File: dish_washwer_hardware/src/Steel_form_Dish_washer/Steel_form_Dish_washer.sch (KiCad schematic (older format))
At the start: 64 parts, among them J1 RTD_TANK_SENSOR, J2 RTD_BOILER_SENSOR, J3 AC_PWR_IN, J4 MAG_DOOR_SENSOR, J5 Conn_01x04_Male, J6 Conn_01x04_Male, J7 FLOAT SWITCH CONN, J8 3-1734592-0, Q1 BSS138, Q2 BSS138, SW1 SW_Push, SW2 SW_Push, SW3 SW_Push, U1 ATmega2560-16AU, U2 LM1117-3.3, U3 MAX31865ATP+T, U4 MAX31865ATP+T, U5 TL1240GQ1JCLR, U6 TL1240GQ1JCLR, Y1 C3E-16.000-12-1010-M

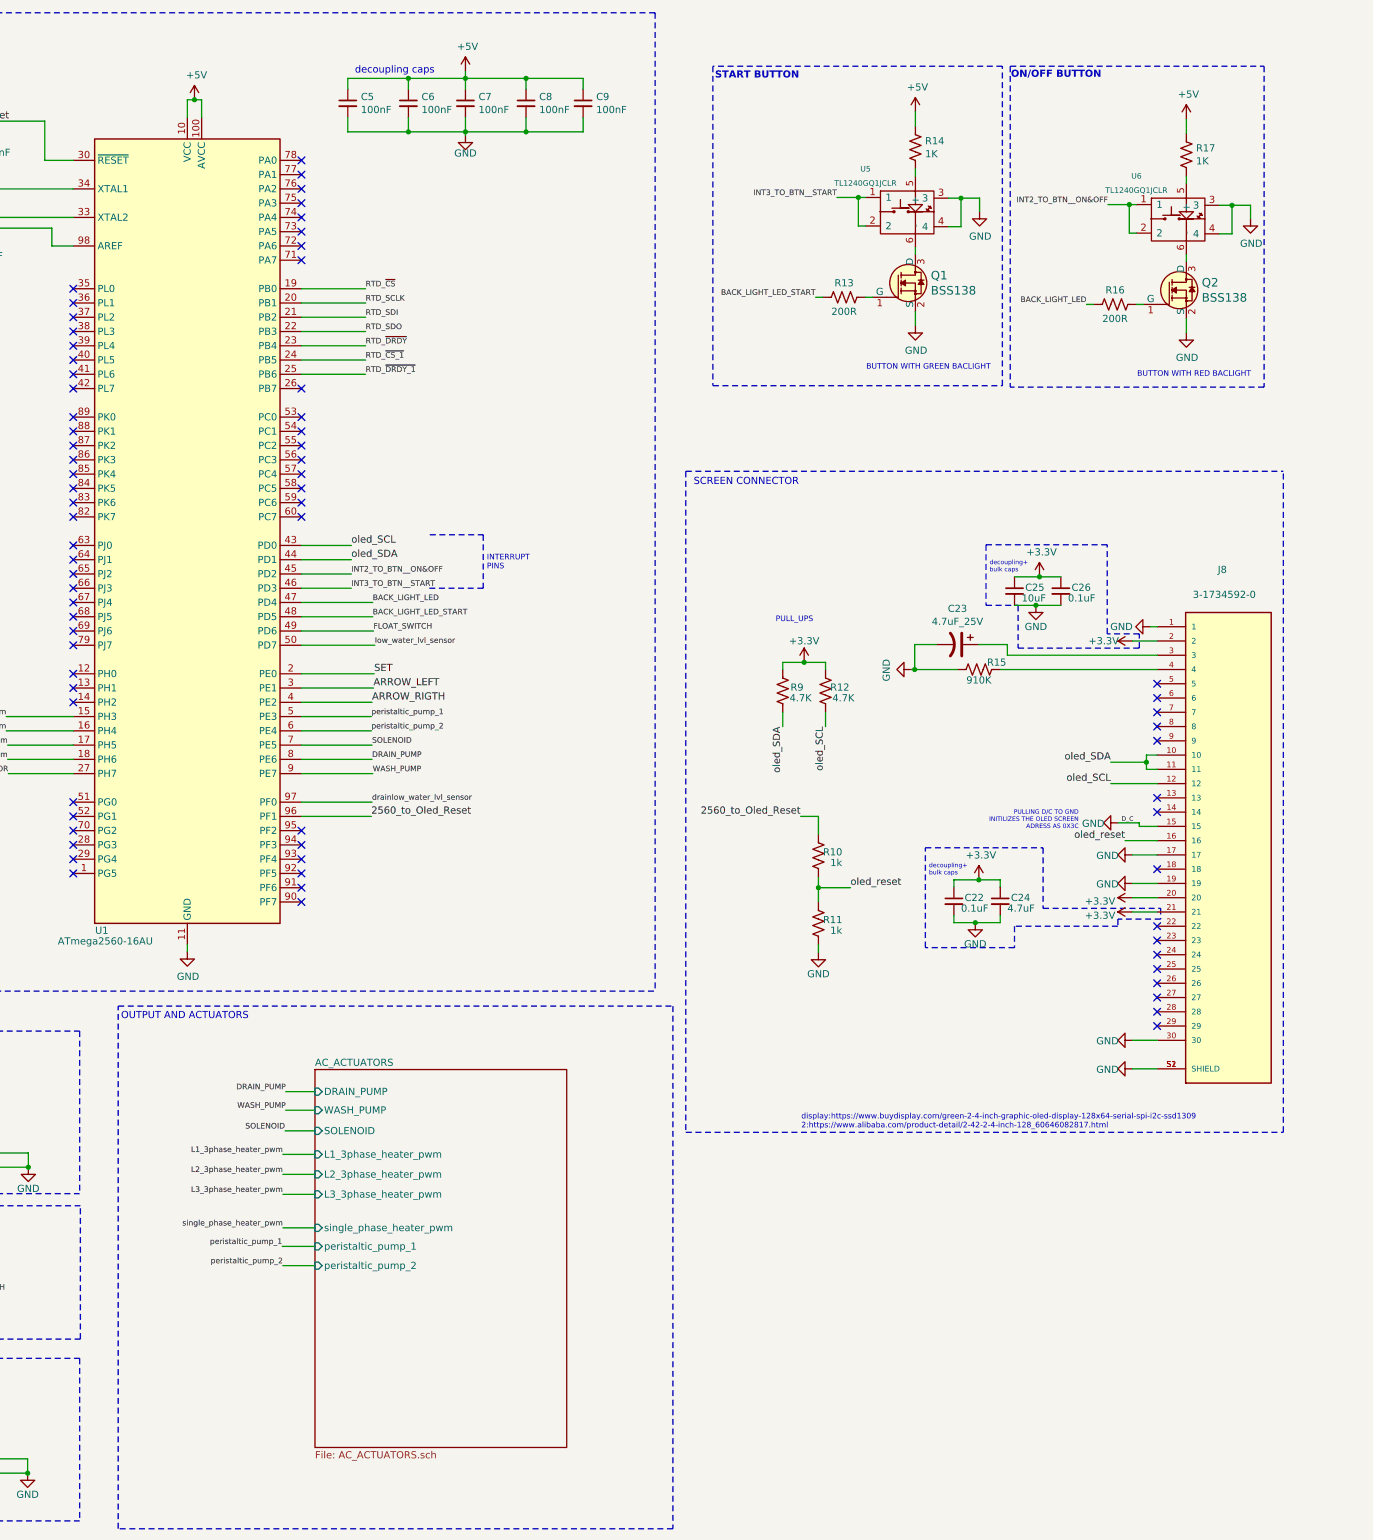
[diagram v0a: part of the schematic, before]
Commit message: update schematic zero detect circuit
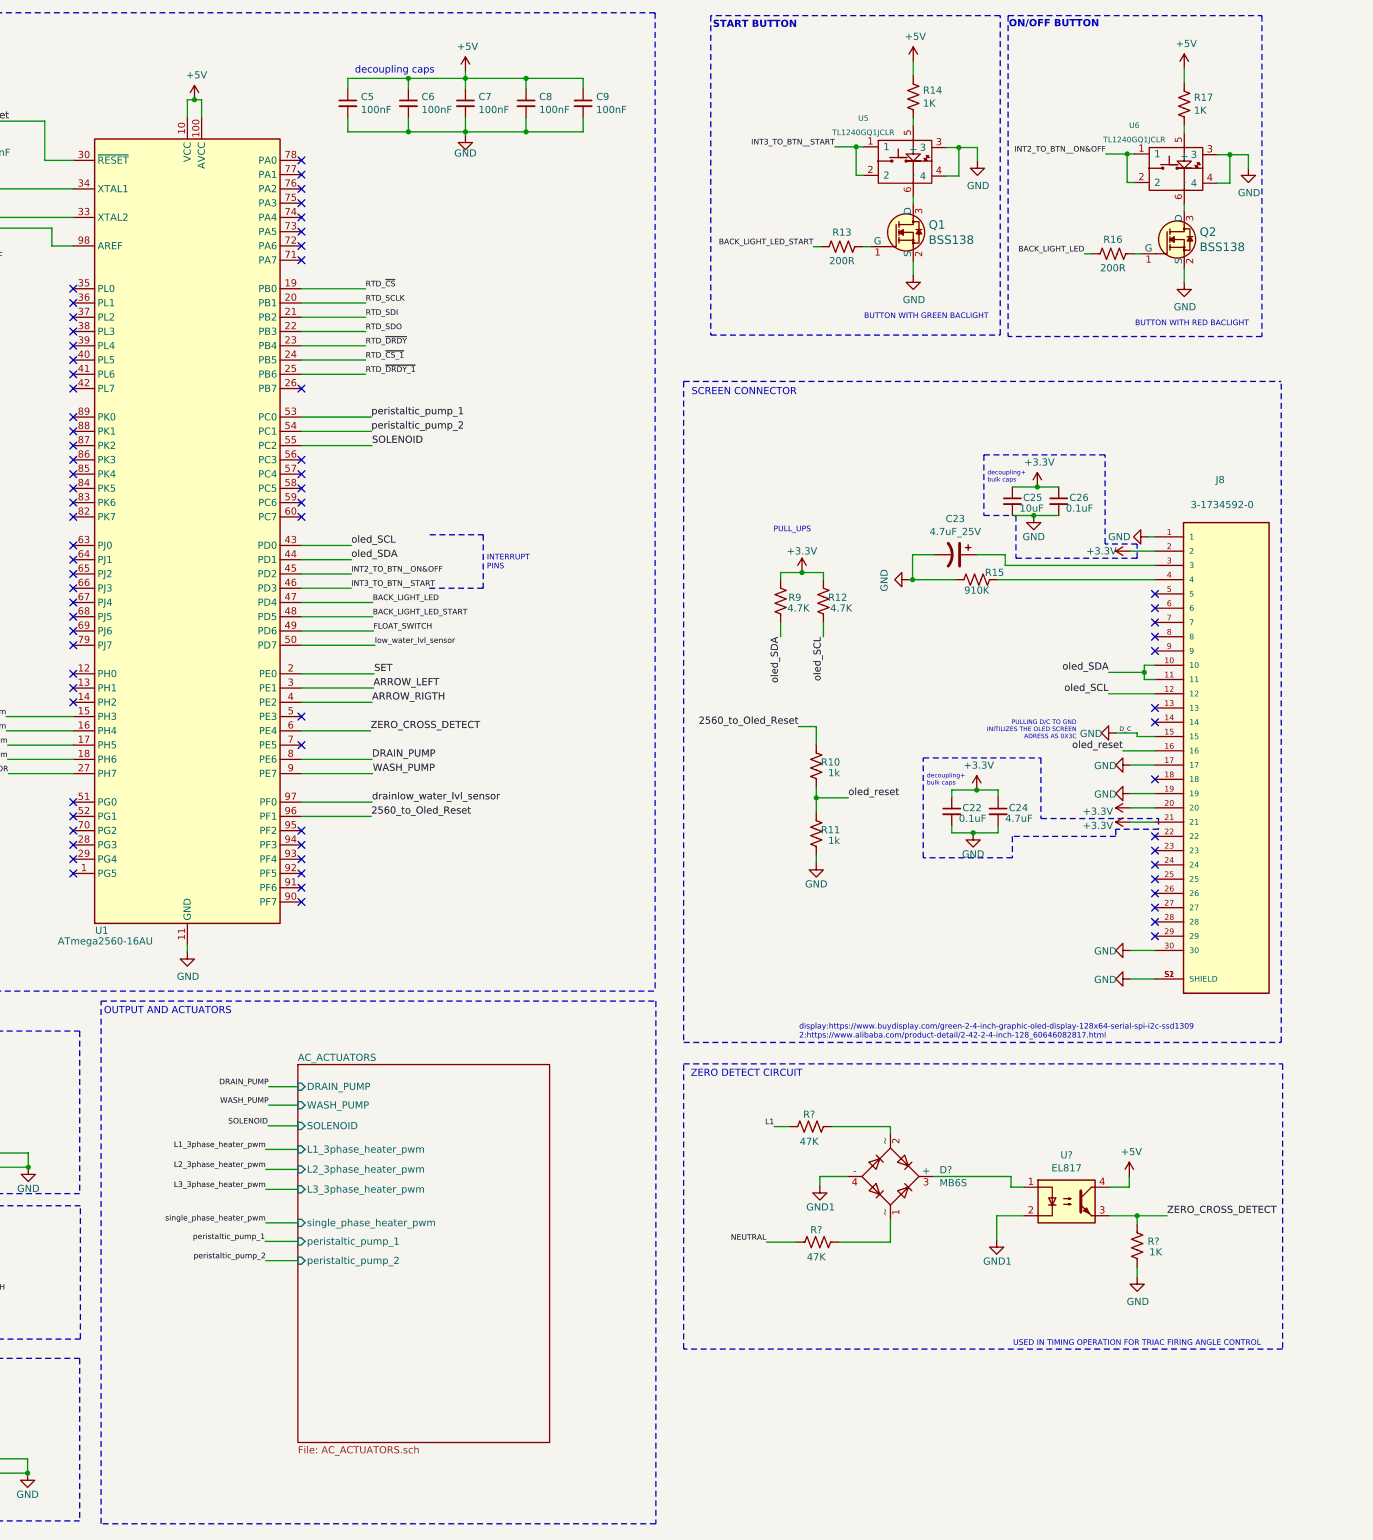
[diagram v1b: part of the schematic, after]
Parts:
- added D?: MB6S, Package_TO_SOT_SMD:TO-269AA, symbol Diode_Bridge:MB6S
- added R? (x2): 47K, symbol Device:R_US
- added R?: 1K, symbol Device:R_US
- added U?: EL817, Package_DIP:DIP-4_W7.62mm, symbol Isolator:EL817
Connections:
- net +5V: now also U?.4
- net GND: now also R?.1
- net L1: now also R?.1
- net NEUTRAL: now also R?.1
- net SOLENOID: now also U1.55 (PC2); no longer U1.7 (PE5)
- net peristaltic_pump_1: now also U1.53 (PC0); no longer U1.5 (PE3)
- net peristaltic_pump_2: now also U1.54 (PC1); no longer U1.6 (PE4)
- new net: D?.1 (~~), R?.2
- new net: D?.2 (~~), R?.2
- new net: D?.3 (+), U?.1
- new net GND1: D?.4 (-), U?.2
- new net ZERO_CROSS_DETECT: R?.2, U1.6 (PE4), U?.3
- no-connect marks 72 -> 71
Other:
- note added: "USED IN TIMING OPERATION FOR TRIAC FIRING ANGLE CONTROL"
- note added: "ZERO DETECT CIRCUIT"
- moved on the sheet: C22, C23, C24, C25, C26, J8, Q1, Q2, R10, R11, R12, R13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

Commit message: footprint assignment and Varistor
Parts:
- added RV1, RV2, RV3: VDR-14D181K, Varistor:RV_Disc_D16.5mm_W6.7mm_P7.5mm, symbol Device:Varistor
- C1, C10, C11, C12, C13, C14, C15, C16, C17, C18, C19, C2, C20, C21, C22, C24, C25, C26, C3, C4, C5, C6, C7, C8, C9: footprint (none) -> Capacitor_SMD:C_0402_1005Metric
- C23: footprint (none) -> Capacitor_Tantalum_SMD:CP_EIA-3528-21_Kemet-B
- J1, J2: footprint (none) -> Connector_JST:JST_EH_S3B-EH_1x03_P2.50mm_Horizontal
- J3: footprint (none) -> greencharge-footprints:387207505
- J4, J7: footprint (none) -> Connector_JST:JST_EH_S2B-EH_1x02_P2.50mm_Horizontal
- J5, J6: footprint (none) -> Connector_JST:JST_EH_S4B-EH_1x04_P2.50mm_Horizontal
- R1, R10, R11, R12, R13, R14, R15, R16, R17, R2, R3, R5, R6, R7, R8, R9: footprint (none) -> Resistor_SMD:R_0402_1005Metric
- R36, R37: renamed from R?; footprint (none) -> Resistor_SMD:R_0805_2012Metric
- R38: renamed from R?; footprint (none) -> Resistor_SMD:R_0402_1005Metric
- R4: value 1K -> 200R; footprint (none) -> Resistor_SMD:R_0402_1005Metric
- gave numbers to parts that had none: 2
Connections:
- net L1: now also RV1.1
- net L2: now also RV2.1
- net L3: now also RV3.1
- net NEUTRAL: now also RV1.2, RV2.2, RV3.2
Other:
- moved on the sheet: J3

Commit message: updated dishwasher schematic
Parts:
- removed J8: 3-1734592-0, greencharge-footprints:TE_3-1734592-0, symbol 3-1734592-0:3-1734592-0
- added J16: Conn_01x31, greencharge-footprints:oled_128x64_GDOE0240G, symbol Connector_Generic:Conn_01x31
- added SW4, SW5: SW_Push, greencharge-footprints:K2-1187SQ-D4SW-06, symbol Switch:SW_Push
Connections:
- net +3V3: now also J16.2 (Pin_2), J16.20 (Pin_20), J16.21 (Pin_21)
- net GND: now also J16.1 (Pin_1), J16.15 (Pin_15), J16.17 (Pin_17), J16.19 (Pin_19), J16.30 (Pin_30), J16.31 (Pin_31), SW4.2, SW5.2
- net oled_SCL: now also J16.12 (Pin_12)
- net oled_SDA: now also J16.10 (Pin_10), J16.11 (Pin_11)
- net oled_reset: now also J16.16 (Pin_16)
- net BACK: now reaches U1.94 (PF3)
- net BACK: now also SW5.1
- net MENU: now reaches U1.95 (PF2)
- net MENU: now also SW4.1
- net at C23.1: now also J16.3 (Pin_3)
- net at R15.1: now also J16.4 (Pin_4)
- no-connect marks 71 -> 69
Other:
- moved on the sheet: SW2
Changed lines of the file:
@@
 	9100 6030 9595 6030
 Wire Notes Line
-	3770 9810 530  9810
-Wire Notes Line
-	3770 8310 3770 9810
-Wire Notes Line
-	530  9810 530  8310
+	3770 10085 530  10085
+Wire Notes Line
+	3770 8310 3770 10085
+Wire Notes Line
+	530  10085 530  8310
 $Comp
 L Switch:SW_Push SW3
@@
 Wire Wire Line
 	2190 8690 2795 8690
-$Comp
-L Switch:SW_Push SW2
-U 1 1 634F85CF
-P 2295 9365
-F 0 "SW2" H 2295 9650 50  0000 C CNN
-F 1 "SW_Push" H 2295 9559 50  0000 C CNN
-F 2 "greencharge-footprints:K2-1187SQ-D4SW-06" H 2295 9565 50  0001 C CNN
-F 3 "~" H 2295 9565 50  0001 C CNN
-	1    2295 9365
-	1    0    0    -1
-$EndComp
-$Comp
-L power:GND #PWR0133
-U 1 1 634F85C5
-P 2725 9440
-F 0 "#PWR0133" H 2725 9190 50  0001 C CNN
-F 1 "GND" H 2725 9290 50  0000 C CNN
-F 2 "" H 2725 9440 50  0001 C CNN
-F 3 "" H 2725 9440 50  0001 C CNN
-	1    2725 9440
-	1    0    0    -1
-$EndComp
-Wire Wire Line
-	2495 9365 2725 9365
-Wire Wire Line
-	2725 9365 2725 9440
-Text Label 1360 9365 0    50   ~ 0
-ARROW_LEFT
-Wire Wire Line
-	1360 9365 2095 9365
 $Comp
 L Switch:SW_Push SW1
@@
 Text Notes 12590 7695 0    39   ~ 0
 display:https://www.buydisplay.com/green-2-4-inch-graphic-oled-display-128x64-serial-spi-i2c-ssd1309\n2:https://www.alibaba.com/product-detail/2-42-2-4-inch-128_60646082817.html\n
-$Comp
-L 3-1734592-0:3-1734592-0 J8
-U 1 1 62278FE9
-P 15585 5670
-F 0 "J8" H 15510 7570 50  0000 L CNN
-F 1 "3-1734592-0" H 15335 7395 50  0000 L CNN
-F 2 "greencharge-footprints:TE_3-1734592-0" H 15585 5670 50  0001 L BNN
-F 3 "" H 15585 5670 50  0001 L BNN
-F 4 "TE Connectivity" H 15585 5670 50  0001 L BNN "MANUFACTURER"
-F 5 "2.05mm" H 15585 5670 50  0001 L BNN "MAXIMUM_PACKAGE_HEIGHT"
-F 6 "Manufacturer Recommendations" H 15585 5670 50  0001 L BNN "STANDARD"
-F 7 "C" H 15585 5670 50  0001 L BNN "PARTREV"
-	1    15585 5670
-	1    0    0    -1
-$EndComp
 Text Notes 7715 7525 0    50   ~ 0
 OUTPUT AND ACTUATORS
@@
 NoConn ~ 15085 6970
 $Comp
-L power:GND #PWR0146
-U 1 1 62734EFB
-P 14910 7270
-F 0 "#PWR0146" H 14910 7020 50  0001 C CNN
-F 1 "GND" V 14915 7097 50  0000 C CNN
-F 2 "" H 14910 7270 50  0001 C CNN
-F 3 "" H 14910 7270 50  0001 C CNN
-	1    14910 7270
-	0    1    1    0
-$EndComp
-Wire Wire Line
-	15085 7270 14910 7270
-$Comp
 L power:GND #PWR0147
 U 1 1 6274D999
@@
 Wire Wire Line
 	9100 4330 9450 4330
-NoConn ~ 9100 6330
-NoConn ~ 9100 6230
 NoConn ~ 9100 6430
 NoConn ~ 9100 6530
@@
 Wire Wire Line
 	1590 2300 1670 2300
+$Comp
+L Connector_Generic:Conn_01x31 J16
+U 1 1 6504CD50
+P 15285 5670
+F 0 "J16" H 15365 5712 50  0000 L CNN
+F 1 "Conn_01x31" H 15365 5621 50  0000 L CNN
+F 2 "greencharge-footprints:oled_128x64_GDOE0240G" H 15285 5670 50  0001 C CNN
+F 3 "~" H 15285 5670 50  0001 C CNN
+	1    15285 5670
+	1    0    0    -1
+$EndComp
+Wire Wire Line
+	15085 7170 14910 7170
+$Comp
+L power:GND #PWR0146
+U 1 1 62734EFB
+P 14910 7170
+F 0 "#PWR0146" H 14910 6920 50  0001 C CNN
+F 1 "GND" V 14915 6997 50  0000 C CNN
+F 2 "" H 14910 7170 50  0001 C CNN
+F 3 "" H 14910 7170 50  0001 C CNN
+	1    14910 7170
+	0    1    1    0
+$EndComp
+$Comp
+L Switch:SW_Push SW2
+U 1 1 634F85CF
+P 2345 9240
+F 0 "SW2" H 2345 9525 50  0000 C CNN
+F 1 "SW_Push" H 2345 9434 50  0000 C CNN
+F 2 "greencharge-footprints:K2-1187SQ-D4SW-06" H 2345 9440 50  0001 C CNN
+F 3 "~" H 2345 9440 50  0001 C CNN
+	1    2345 9240
+	1    0    0    -1
+$EndComp
+$Comp
+L power:GND #PWR0133
+U 1 1 634F85C5
+P 2675 9315
+F 0 "#PWR0133" H 2675 9065 50  0001 C CNN
+F 1 "GND" H 2675 9165 50  0000 C CNN
+F 2 "" H 2675 9315 50  0001 C CNN
+F 3 "" H 2675 9315 50  0001 C CNN
+	1    2675 9315
+	1    0    0    -1
+$EndComp
+Wire Wire Line
+	2545 9240 2675 9240
+Wire Wire Line
+	2675 9240 2675 9315
+Text Label 1635 9240 0    50   ~ 0
+ARROW_LEFT
+Wire Wire Line
+	1635 9240 2145 9240
+$Comp
+L Switch:SW_Push SW4
+U 1 1 61EAB204
+P 1470 9740
+F 0 "SW4" H 1470 10025 50  0000 C CNN
+F 1 "SW_Push" H 1470 9934 50  0000 C CNN
+F 2 "greencharge-footprints:K2-1187SQ-D4SW-06" H 1470 9940 50  0001 C CNN
+F 3 "~" H 1470 9940 50  0001 C CNN
+	1    1470 9740
+	1    0    0    -1
+$EndComp
+$Comp
+L power:GND #PWR01
+U 1 1 61EAB220
+P 1800 9815
+F 0 "#PWR01" H 1800 9565 50  0001 C CNN
+F 1 "GND" H 1800 9665 50  0000 C CNN
+F 2 "" H 1800 9815 50  0001 C CNN
+F 3 "" H 1800 9815 50  0001 C CNN
+	1    1800 9815
+	1    0    0    -1
+$EndComp
+Wire Wire Line
+	1670 9740 1800 9740
+Wire Wire Line
+	1800 9740 1800 9815
+Text Label 760  9740 0    50   ~ 0
+MENU
+Wire Wire Line
+	760  9740 1270 9740
+$Comp
+L Switch:SW_Push SW5
+U 1 1 61ECFB0D
+P 3195 9790
+F 0 "SW5" H 3195 10075 50  0000 C CNN
+F 1 "SW_Push" H 3195 9984 50  0000 C CNN
+F 2 "greencharge-footprints:K2-1187SQ-D4SW-06" H 3195 9990 50  0001 C CNN
+F 3 "~" H 3195 9990 50  0001 C CNN
+	1    3195 9790
+	1    0    0    -1
+$EndComp
+$Comp
+L power:GND #PWR02
+U 1 1 61ECFB29
+P 3525 9865
+F 0 "#PWR02" H 3525 9615 50  0001 C CNN
+F 1 "GND" H 3525 9715 50  0000 C CNN
+F 2 "" H 3525 9865 50  0001 C CNN
+F 3 "" H 3525 9865 50  0001 C CNN
+	1    3525 9865
+	1    0    0    -1
+$EndComp
+Wire Wire Line
+	3395 9790 3525 9790
+Wire Wire Line
+	3525 9790 3525 9865
+Text Label 2485 9790 0    50   ~ 0
+BACK
+Wire Wire Line
+	2485 9790 2995 9790
+Text Label 9585 6230 0    50   ~ 0
+MENU
+Text Label 9585 6330 0    50   ~ 0
+BACK
+Wire Wire Line
+	9100 6230 9585 6230
+Wire Wire Line
+	9100 6330 9585 6330
 $EndSCHEMATC
